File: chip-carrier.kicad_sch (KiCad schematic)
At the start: 9 parts, among them U1 Contact_Pad, U2 Contact_Pad, U3 Contact_Pad, U4 Contact_Pad, U5 Gate_Pad, U6 Contact_Pad, U7 Contact_Pad, U8 Contact_Pad, U9 Contact_Pad

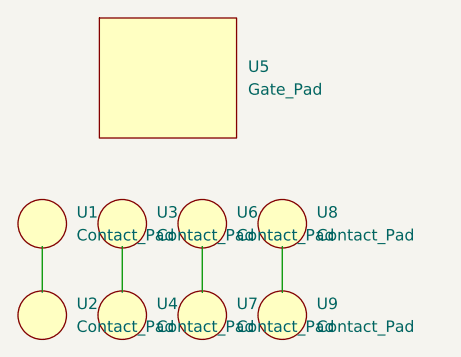
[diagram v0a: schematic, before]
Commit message: Redesign contact pads
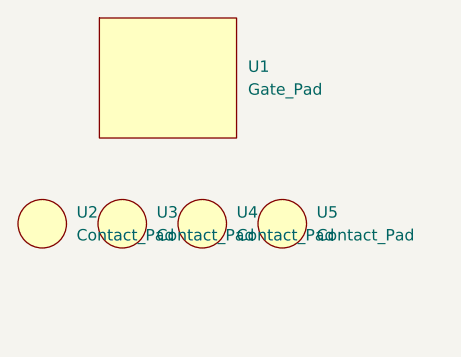
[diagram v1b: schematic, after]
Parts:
- removed U2, U4, U7, U9: Contact_Pad, Chip_Carrier:C1500, symbol Chip_Carrier:Contact_Pad
- U1: renamed from U5; footprint Chip_Carrier:R12000X10000 -> chip_carrier:R12000X10000
- U2: renamed from U1; footprint Chip_Carrier:C1500 -> chip_carrier:C2500
- U3: footprint Chip_Carrier:C1500 -> chip_carrier:C2500
- U4: renamed from U6; footprint Chip_Carrier:C1500 -> chip_carrier:C2500
- U5: renamed from U8; footprint Chip_Carrier:C1500 -> chip_carrier:C2500
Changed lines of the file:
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@@
     (comment 4 "Author: Justin Zhou Yong")
-  )
-  (wire (pts (xy 146.05 106.68) (xy 146.05 111.76))
-    (stroke (width 0) (type default) (color 0 0 0 0))
-  )
-  (wire (pts (xy 137.16 106.68) (xy 137.16 111.76))
-    (stroke (width 0) (type default) (color 0 0 0 0))
-  )
-  (wire (pts (xy 128.27 106.68) (xy 128.27 111.76))
-    (stroke (width 0) (type default) (color 0 0 0 0))
-  )
-  (wire (pts (xy 154.94 106.68) (xy 154.94 111.76))
-    (stroke (width 0) (type default) (color 0 0 0 0))
-  )
-  (symbol (lib_id "Chip_Carrier:Contact_Pad") (at 137.16 114.3 0) (unit 1)
-    (in_bom yes) (on_board yes) (fields_autoplaced)
-    (property "Reference" "U4" (id 0) (at 140.97 113.0299 0)
-      (effects (font (size 1.27 1.27)) (justify left))
-    )
-    (property "Value" "Contact_Pad" (id 1) (at 140.97 115.5699 0)
-      (effects (font (size 1.27 1.27)) (justify left))
-    )
-    (property "Footprint" "Chip_Carrier:C1500" (id 2) (at 137.16 114.3 0)
-      (effects (font (size 1.27 1.27)) hide)
-    )
-    (property "Datasheet" "" (id 3) (at 137.16 114.3 0)
-      (effects (font (size 1.27 1.27)) hide)
-    )
-  )
-  (symbol (lib_id "Chip_Carrier:Contact_Pad") (at 146.05 114.3 0) (unit 1)
-    (in_bom yes) (on_board yes) (fields_autoplaced)
-    (property "Reference" "U7" (id 0) (at 149.86 113.0299 0)
-      (effects (font (size 1.27 1.27)) (justify left))
-    )
-    (property "Value" "Contact_Pad" (id 1) (at 149.86 115.5699 0)
-      (effects (font (size 1.27 1.27)) (justify left))
-    )
-    (property "Footprint" "Chip_Carrier:C1500" (id 2) (at 146.05 114.3 0)
-      (effects (font (size 1.27 1.27)) hide)
-    )
-    (property "Datasheet" "" (id 3) (at 146.05 114.3 0)
-      (effects (font (size 1.27 1.27)) hide)
-    )
   )
   (symbol (lib_id "Chip_Carrier:Contact_Pad") (at 146.05 104.14 0) (unit 1)
     (in_bom yes) (on_board yes) (fields_autoplaced)
-    (property "Reference" "U6" (id 0) (at 149.86 102.8699 0)
+    (property "Reference" "U4" (id 0) (at 149.86 102.8699 0)
       (effects (font (size 1.27 1.27)) (justify left))
     )
@@
       (effects (font (size 1.27 1.27)) (justify left))
     )
-    (property "Footprint" "Chip_Carrier:C1500" (id 2) (at 146.05 104.14 0)
+    (property "Footprint" "chip_carrier:C2500" (id 2) (at 146.05 104.14 0)
       (effects (font (size 1.27 1.27)) hide)
     )
@@
   (symbol (lib_id "Chip_Carrier:Contact_Pad") (at 154.94 104.14 0) (unit 1)
     (in_bom yes) (on_board yes) (fields_autoplaced)
-    (property "Reference" "U8" (id 0) (at 158.75 102.8699 0)
+    (property "Reference" "U5" (id 0) (at 158.75 102.8699 0)
       (effects (font (size 1.27 1.27)) (justify left))
     )
@@
       (effects (font (size 1.27 1.27)) (justify left))
     )
-    (property "Footprint" "Chip_Carrier:C1500" (id 2) (at 154.94 104.14 0)
+    (property "Footprint" "chip_carrier:C2500" (id 2) (at 154.94 104.14 0)
       (effects (font (size 1.27 1.27)) hide)
     )
@@
   (symbol (lib_id "Chip_Carrier:Contact_Pad") (at 128.27 104.14 0) (unit 1)
     (in_bom yes) (on_board yes) (fields_autoplaced)
-    (property "Reference" "U1" (id 0) (at 132.08 102.8699 0)
+    (property "Reference" "U2" (id 0) (at 132.08 102.8699 0)
       (effects (font (size 1.27 1.27)) (justify left))
     )
@@
       (effects (font (size 1.27 1.27)) (justify left))
     )
-    (property "Footprint" "Chip_Carrier:C1500" (id 2) (at 128.27 104.14 0)
+    (property "Footprint" "chip_carrier:C2500" (id 2) (at 128.27 104.14 0)
       (effects (font (size 1.27 1.27)) hide)
     )
     (property "Datasheet" "" (id 3) (at 128.27 104.14 0)
-      (effects (font (size 1.27 1.27)) hide)
-    )
-  )
-  (symbol (lib_id "Chip_Carrier:Contact_Pad") (at 154.94 114.3 0) (unit 1)
-    (in_bom yes) (on_board yes) (fields_autoplaced)
-    (property "Reference" "U9" (id 0) (at 158.75 113.0299 0)
-      (effects (font (size 1.27 1.27)) (justify left))
-    )
-    (property "Value" "Contact_Pad" (id 1) (at 158.75 115.5699 0)
-      (effects (font (size 1.27 1.27)) (justify left))
-    )
-    (property "Footprint" "Chip_Carrier:C1500" (id 2) (at 154.94 114.3 0)
-      (effects (font (size 1.27 1.27)) hide)
-    )
-    (property "Datasheet" "" (id 3) (at 154.94 114.3 0)
       (effects (font (size 1.27 1.27)) hide)
     )
@@
       (effects (font (size 1.27 1.27)) (justify left))
     )
-    (property "Footprint" "Chip_Carrier:C1500" (id 2) (at 137.16 104.14 0)
+    (property "Footprint" "chip_carrier:C2500" (id 2) (at 137.16 104.14 0)
       (effects (font (size 1.27 1.27)) hide)
     )
@@
     )
   )
-  (symbol (lib_id "Chip_Carrier:Contact_Pad") (at 128.27 114.3 0) (unit 1)
-    (in_bom yes) (on_board yes) (fields_autoplaced)
-    (property "Reference" "U2" (id 0) (at 132.08 113.0299 0)
-      (effects (font (size 1.27 1.27)) (justify left))
-    )
-    (property "Value" "Contact_Pad" (id 1) (at 132.08 115.5699 0)
-      (effects (font (size 1.27 1.27)) (justify left))
-    )
-    (property "Footprint" "Chip_Carrier:C1500" (id 2) (at 128.27 114.3 0)
-      (effects (font (size 1.27 1.27)) hide)
-    )
-    (property "Datasheet" "" (id 3) (at 128.27 114.3 0)
-      (effects (font (size 1.27 1.27)) hide)
-    )
-  )
   (symbol (lib_id "Chip_Carrier:Gate_Pad") (at 142.24 87.63 0) (unit 1)
     (in_bom yes) (on_board yes) (fields_autoplaced)
-    (property "Reference" "U5" (id 0) (at 151.13 86.6774 0)
+    (property "Reference" "U1" (id 0) (at 151.13 86.6774 0)
       (effects (font (size 1.27 1.27)) (justify left))
     )
@@
       (effects (font (size 1.27 1.27)) (justify left))
     )
-    (property "Footprint" "Chip_Carrier:R12000X10000" (id 2) (at 142.24 87.63 0)
+    (property "Footprint" "chip_carrier:R12000X10000" (id 2) (at 142.24 87.63 0)
       (effects (font (size 1.27 1.27)) hide)
     )
@@
   )
   (symbol_instances
+    (path "/fc7abe25-5188-43f4-acd9-3096e88cea1f"
+      (reference "U1") (unit 1) (value "Gate_Pad") (footprint "chip_carrier:R12000X10000")
+    )
     (path "/89c6b43b-111d-4b9e-a4e2-05335a31aa9b"
-      (reference "U1") (unit 1) (value "Contact_Pad") (footprint "Chip_Carrier:C1500")
-    )
-    (path "/d11a2a9e-7af4-4e9c-ab11-4d2cbd518321"
-      (reference "U2") (unit 1) (value "Contact_Pad") (footprint "Chip_Carrier:C1500")
+      (reference "U2") (unit 1) (value "Contact_Pad") (footprint "chip_carrier:C2500")
     )
     (path "/c285188a-145c-43b8-8e58-5b66b3ce40e7"
-      (reference "U3") (unit 1) (value "Contact_Pad") (footprint "Chip_Carrier:C1500")
-    )
-    (path "/172b4d51-1b93-4970-9651-718ca50c793c"
-      (reference "U4") (unit 1) (value "Contact_Pad") (footprint "Chip_Carrier:C1500")
-    )
-    (path "/fc7abe25-5188-43f4-acd9-3096e88cea1f"
-      (reference "U5") (unit 1) (value "Gate_Pad") (footprint "Chip_Carrier:R12000X10000")
+      (reference "U3") (unit 1) (value "Contact_Pad") (footprint "chip_carrier:C2500")
     )
     (path "/6cc860dc-8b7e-4c9e-b73d-0adb22af97d6"
-      (reference "U6") (unit 1) (value "Contact_Pad") (footprint "Chip_Carrier:C1500")
-    )
-    (path "/557a851f-102d-4680-bf50-11b56ee55c32"
-      (reference "U7") (unit 1) (value "Contact_Pad") (footprint "Chip_Carrier:C1500")
+      (reference "U4") (unit 1) (value "Contact_Pad") (footprint "chip_carrier:C2500")
     )
     (path "/78070258-bbd8-449c-83f4-3cd3cb922c8f"
-      (reference "U8") (unit 1) (value "Contact_Pad") (footprint "Chip_Carrier:C1500")
-    )
-    (path "/a7242bf7-10ab-4fd7-b379-c6354d45c738"
-      (reference "U9") (unit 1) (value "Contact_Pad") (footprint "Chip_Carrier:C1500")
+      (reference "U5") (unit 1) (value "Contact_Pad") (footprint "chip_carrier:C2500")
     )
   )

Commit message: Change contact pads to rounded rectangular shape
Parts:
- U2, U3, U4, U5: footprint chip_carrier:C2500 -> chip_carrier:R2000X3000
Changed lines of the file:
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@@
       (effects (font (size 1.27 1.27)) (justify left))
     )
-    (property "Footprint" "chip_carrier:C2500" (id 2) (at 146.05 104.14 0)
+    (property "Footprint" "chip_carrier:R2000X3000" (id 2) (at 146.05 104.14 0)
       (effects (font (size 1.27 1.27)) hide)
     )
@@
       (effects (font (size 1.27 1.27)) (justify left))
     )
-    (property "Footprint" "chip_carrier:C2500" (id 2) (at 154.94 104.14 0)
+    (property "Footprint" "chip_carrier:R2000X3000" (id 2) (at 154.94 104.14 0)
       (effects (font (size 1.27 1.27)) hide)
     )
@@
       (effects (font (size 1.27 1.27)) (justify left))
     )
-    (property "Footprint" "chip_carrier:C2500" (id 2) (at 128.27 104.14 0)
+    (property "Footprint" "chip_carrier:R2000X3000" (id 2) (at 128.27 104.14 0)
       (effects (font (size 1.27 1.27)) hide)
     )
@@
       (effects (font (size 1.27 1.27)) (justify left))
     )
-    (property "Footprint" "chip_carrier:C2500" (id 2) (at 137.16 104.14 0)
+    (property "Footprint" "chip_carrier:R2000X3000" (id 2) (at 137.16 104.14 0)
       (effects (font (size 1.27 1.27)) hide)
     )
@@
     )
     (path "/89c6b43b-111d-4b9e-a4e2-05335a31aa9b"
-      (reference "U2") (unit 1) (value "Contact_Pad") (footprint "chip_carrier:C2500")
+      (reference "U2") (unit 1) (value "Contact_Pad") (footprint "chip_carrier:R2000X3000")
     )
     (path "/c285188a-145c-43b8-8e58-5b66b3ce40e7"
-      (reference "U3") (unit 1) (value "Contact_Pad") (footprint "chip_carrier:C2500")
+      (reference "U3") (unit 1) (value "Contact_Pad") (footprint "chip_carrier:R2000X3000")
     )
     (path "/6cc860dc-8b7e-4c9e-b73d-0adb22af97d6"
-      (reference "U4") (unit 1) (value "Contact_Pad") (footprint "chip_carrier:C2500")
+      (reference "U4") (unit 1) (value "Contact_Pad") (footprint "chip_carrier:R2000X3000")
     )
     (path "/78070258-bbd8-449c-83f4-3cd3cb922c8f"
-      (reference "U5") (unit 1) (value "Contact_Pad") (footprint "chip_carrier:C2500")
+      (reference "U5") (unit 1) (value "Contact_Pad") (footprint "chip_carrier:R2000X3000")
     )
   )
